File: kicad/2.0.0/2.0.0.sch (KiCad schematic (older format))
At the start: 66 parts

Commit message: assignd footprints to schematic, grouped footprints in pcb designer
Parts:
- C1, C10, C11, C12, C13, C14, C15, C16, C17, C18, C2, C3, C4, C5, C6, C9: renamed from C?; footprint (none) -> Capacitor_SMD:C_0603_1608Metric
- C7, C8: renamed from C?; footprint (none) -> Capacitor_SMD:C_1206_3216Metric
- D1: renamed from D?; footprint (none) -> Sensor_Optical_Position:S5990; symbol Sensor_Optical_Position:S599x -> 2.0.0-rescue:S599x-Sensor_Optical_Position
- J1, J2, J4: renamed from J?; footprint (none) -> Connector_SMA:SMA_Molex_73251-2120_EdgeMount
- J3: renamed from J?; footprint (none) -> TerminalBlock_TE-Connectivity:TerminalBlock_TE_282834-3_1x03_P2.54mm_Horizontal
- R1, R10, R11, R12, R13, R14, R15, R16, R17, R18, R19, R2, R20, R21, R22, R23, R24, R25, R26, R3, R4, R5, R6, R7, R8, R9: renamed from R?; footprint (none) -> Resistor_SMD:R_0603_1608Metric
- U1, U2, U5, U6: renamed from U?; footprint (none) -> Package_SO:SOIC-8_3.9x4.9mm_P1.27mm
- U3: renamed from U?; footprint (none) -> Package_TO_SOT_SMD:SOT-223-3_TabPin2
- gave numbers to parts that had none: 1

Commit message: updated footprints of S5990, OPA197 and OPA2197
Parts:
- removed U1, U2, U5: OPA2197, Package_SO:SOIC-8_3.9x4.9mm_P1.27mm, symbol Device:Opamp_Dual_Generic
- removed U6: OPA197, Package_SO:SOIC-8_3.9x4.9mm_P1.27mm, symbol Device:Opamp_Dual_Generic
- added U1, U2, U5: OPA2197IDR, Package_SO:SOIC-8_3.9x4.9mm_P1.27mm, symbol Amplifier_Operational:OPA2197IDR
- added U6: OPA197IDR, Package_SO:SOIC-8_3.9x4.9mm_P1.27mm, symbol Amplifier_Operational:OPA197IDR
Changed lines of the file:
@@
-	1    0    0    -1
-$EndComp
-$Comp
-L Device:Opamp_Dual_Generic U1
-U 1 1 5E395987
-P 2250 1850
-F 0 "U1" H 2250 1483 50  0000 C CNN
-F 1 "OPA2197" H 2250 1574 50  0000 C CNN
-F 2 "Package_SO:SOIC-8_3.9x4.9mm_P1.27mm" H 2250 1850 50  0001 C CNN
-F 3 "~" H 2250 1850 50  0001 C CNN
-	1    2250 1850
-	1    0    0    1
-$EndComp
-$Comp
-L Device:Opamp_Dual_Generic U1
-U 2 1 5E396064
-P 3750 1850
-F 0 "U1" H 3750 1483 50  0000 C CNN
-F 1 "OPA2197" H 3750 1574 50  0000 C CNN
-F 2 "Package_SO:SOIC-8_3.9x4.9mm_P1.27mm" H 3750 1850 50  0001 C CNN
-F 3 "~" H 3750 1850 50  0001 C CNN
-	2    3750 1850
-	1    0    0    1
-$EndComp
-$Comp
-L Device:Opamp_Dual_Generic U1
-U 3 1 5E39666A
-P 950 1550
-F 0 "U1" H 1000 1650 50  0000 L CNN
-F 1 "OPA2197" H 900 1550 50  0000 L CNN
-F 2 "Package_SO:SOIC-8_3.9x4.9mm_P1.27mm" H 950 1550 50  0001 C CNN
-F 3 "~" H 950 1550 50  0001 C CNN
-	3    950  1550
 	1    0    0    -1
 $EndComp
@@
 Wire Wire Line
 	850  3850 850  3700
-$Comp
-L Device:Opamp_Dual_Generic U2
-U 1 1 5E3E1751
-P 2250 3600
-F 0 "U2" H 2250 3233 50  0000 C CNN
-F 1 "OPA2197" H 2250 3324 50  0000 C CNN
-F 2 "Package_SO:SOIC-8_3.9x4.9mm_P1.27mm" H 2250 3600 50  0001 C CNN
-F 3 "~" H 2250 3600 50  0001 C CNN
-	1    2250 3600
-	1    0    0    1
-$EndComp
-$Comp
-L Device:Opamp_Dual_Generic U2
-U 2 1 5E3E290A
-P 3750 3600
-F 0 "U2" H 3750 3233 50  0000 C CNN
-F 1 "OPA2197" H 3750 3324 50  0000 C CNN
-F 2 "Package_SO:SOIC-8_3.9x4.9mm_P1.27mm" H 3750 3600 50  0001 C CNN
-F 3 "~" H 3750 3600 50  0001 C CNN
-	2    3750 3600
-	1    0    0    1
-$EndComp
-$Comp
-L Device:Opamp_Dual_Generic U2
-U 3 1 5E3E3958
-P 950 3300
-F 0 "U2" H 1000 3400 50  0000 L CNN
-F 1 "OPA2197" H 900 3300 50  0000 L CNN
-F 2 "Package_SO:SOIC-8_3.9x4.9mm_P1.27mm" H 950 3300 50  0001 C CNN
-F 3 "~" H 950 3300 50  0001 C CNN
-	3    950  3300
-	1    0    0    -1
-$EndComp
 Wire Wire Line
 	1200 4550 1000 4550
@@
 Text Notes 2200 4650 0    42   Italic 0
 For details on how to size the feedback capacitor check\nW. Jung. Opamp Application Handbook. p. 273
-$Comp
-L Device:Opamp_Dual_Generic U5
-U 1 1 5E43D5EA
-P 6950 1500
-F 0 "U5" H 6950 1133 50  0000 C CNN
-F 1 "OPA2197" H 6950 1224 50  0000 C CNN
-F 2 "Package_SO:SOIC-8_3.9x4.9mm_P1.27mm" H 6950 1500 50  0001 C CNN
-F 3 "~" H 6950 1500 50  0001 C CNN
-	1    6950 1500
-	1    0    0    1
-$EndComp
-$Comp
-L Device:Opamp_Dual_Generic U5
-U 2 1 5E43E84F
-P 6950 3300
-F 0 "U5" H 6950 2933 50  0000 C CNN
-F 1 "OPA2197" H 6950 3024 50  0000 C CNN
-F 2 "Package_SO:SOIC-8_3.9x4.9mm_P1.27mm" H 6950 3300 50  0001 C CNN
-F 3 "~" H 6950 3300 50  0001 C CNN
-	2    6950 3300
-	1    0    0    1
-$EndComp
-$Comp
-L Device:Opamp_Dual_Generic U5
-U 3 1 5E43F028
-P 5300 2500
-F 0 "U5" H 5050 2450 50  0000 R CNN
-F 1 "OPA2197" H 5100 2550 50  0000 R CNN
-F 2 "Package_SO:SOIC-8_3.9x4.9mm_P1.27mm" H 5300 2500 50  0001 C CNN
-F 3 "~" H 5300 2500 50  0001 C CNN
-	3    5300 2500
-	-1   0    0    1
-$EndComp
 $Comp
 L power:GND #PWR0117
@@
 Text Notes 5600 4600 0    42   Italic 0
 See the S5990 datasheet for details on the formula.
-$Comp
-L Device:Opamp_Dual_Generic U6
-U 1 1 5E6E4B30
-P 10200 1600
-F 0 "U6" H 10200 1233 50  0000 C CNN
-F 1 "OPA197" H 10200 1324 50  0000 C CNN
-F 2 "Package_SO:SOIC-8_3.9x4.9mm_P1.27mm" H 10200 1600 50  0001 C CNN
-F 3 "~" H 10200 1600 50  0001 C CNN
-	1    10200 1600
-	1    0    0    1
-$EndComp
 Text Label 9200 1100 0    50   Italic 0
 -X1
@@
 See the S5990 datasheet for details on the formula.
 Connection ~ 10600 1600
-$Comp
-L Device:Opamp_Dual_Generic U6
-U 3 1 5E764FFA
-P 8700 1950
-F 0 "U6" H 8658 1996 50  0000 L CNN
-F 1 "OPA197" H 8658 1905 50  0000 L CNN
-F 2 "Package_SO:SOIC-8_3.9x4.9mm_P1.27mm" H 8700 1950 50  0001 C CNN
-F 3 "~" H 8700 1950 50  0001 C CNN
-	3    8700 1950
-	1    0    0    -1
-$EndComp
 $Comp
 L power:+12V #PWR0129
@@
 Text Notes 3550 6750 0    50   ~ 0
 OUTPUT CONNECTORS
+$Comp
+L Amplifier_Operational:OPA197IDR U6
+U 2 1 5E3ED93E
+P 8600 1950
+F 0 "U6" H 8850 2000 50  0000 C CNN
+F 1 "OPA197IDR" H 8850 1900 50  0000 C CNN
+F 2 "Package_SO:SOIC-8_3.9x4.9mm_P1.27mm" H 8650 1950 50  0001 C CNN
+F 3 "" H 8650 1950 50  0001 C CNN
+	2    8600 1950
+	1    0    0    -1
+$EndComp
+$Comp
+L Amplifier_Operational:OPA197IDR U6
+U 1 1 5E3EEBF9
+P 10150 1600
+F 0 "U6" H 10250 1750 50  0000 L CNN
+F 1 "OPA197IDR" H 10200 1400 50  0000 L CNN
+F 2 "Package_SO:SOIC-8_3.9x4.9mm_P1.27mm" H 10200 1600 50  0001 C CNN
+F 3 "" H 10200 1600 50  0001 C CNN
+	1    10150 1600
+	1    0    0    -1
+$EndComp
+$Comp
+L Amplifier_Operational:OPA2197IDR U5
+U 2 1 5E495054
+P 6900 3300
+F 0 "U5" H 7100 3450 50  0000 C CNN
+F 1 "OPA2197IDR" H 7100 3100 50  0000 C CNN
+F 2 "Package_SO:SOIC-8_3.9x4.9mm_P1.27mm" H 6950 3500 50  0001 C CNN
+F 3 "~" H 6950 3500 50  0001 C CNN
+	2    6900 3300
+	1    0    0    -1
+$EndComp
+$Comp
+L Amplifier_Operational:OPA2197IDR U5
+U 3 1 5E4964C0
+P 5500 2500
+F 0 "U5" H 5600 2550 50  0000 L CNN
+F 1 "OPA2197IDR" H 5458 2455 50  0000 L CNN
+F 2 "Package_SO:SOIC-8_3.9x4.9mm_P1.27mm" H 5550 2700 50  0001 C CNN
+F 3 "~" H 5550 2700 50  0001 C CNN
+	3    5500 2500
+	1    0    0    -1
+$EndComp
+$Comp
+L Amplifier_Operational:OPA2197IDR U1
+U 1 1 5E4983D9
+P 2200 1850
+F 0 "U1" H 2350 2050 50  0000 C CNN
+F 1 "OPA2197IDR" H 2450 1650 50  0000 C CNN
+F 2 "Package_SO:SOIC-8_3.9x4.9mm_P1.27mm" H 2250 2050 50  0001 C CNN
+F 3 "~" H 2250 2050 50  0001 C CNN
+	1    2200 1850
+	1    0    0    -1
+$EndComp
+$Comp
+L Amplifier_Operational:OPA2197IDR U1
+U 2 1 5E4995C9
+P 3700 1850
+F 0 "U1" H 3850 2050 50  0000 C CNN
+F 1 "OPA2197IDR" H 3950 1650 50  0000 C CNN
+F 2 "Package_SO:SOIC-8_3.9x4.9mm_P1.27mm" H 3750 2050 50  0001 C CNN
+F 3 "~" H 3750 2050 50  0001 C CNN
+	2    3700 1850
+	1    0    0    -1
+$EndComp
+$Comp
+L Amplifier_Operational:OPA2197IDR U1
+U 3 1 5E49A8CC
+P 950 1550
+F 0 "U1" H 1050 1650 50  0000 L CNN
+F 1 "OPA2197IDR" H 900 1550 50  0000 L CNN
+F 2 "Package_SO:SOIC-8_3.9x4.9mm_P1.27mm" H 1000 1750 50  0001 C CNN
+F 3 "~" H 1000 1750 50  0001 C CNN
+	3    950  1550
+	1    0    0    -1
+$EndComp
+$Comp
+L Amplifier_Operational:OPA2197IDR U2
+U 1 1 5E4A737B
+P 2200 3600
+F 0 "U2" H 2350 3800 50  0000 C CNN
+F 1 "OPA2197IDR" H 2500 3400 50  0000 C CNN
+F 2 "Package_SO:SOIC-8_3.9x4.9mm_P1.27mm" H 2250 3800 50  0001 C CNN
+F 3 "~" H 2250 3800 50  0001 C CNN
+	1    2200 3600
+	1    0    0    -1
+$EndComp
+$Comp
+L Amplifier_Operational:OPA2197IDR U2
+U 2 1 5E4A876E
+P 3700 3600
+F 0 "U2" H 3800 3800 50  0000 C CNN
+F 1 "OPA2197IDR" H 4000 3400 50  0000 C CNN
+F 2 "Package_SO:SOIC-8_3.9x4.9mm_P1.27mm" H 3750 3800 50  0001 C CNN
+F 3 "~" H 3750 3800 50  0001 C CNN
+	2    3700 3600
+	1    0    0    -1
+$EndComp
+$Comp
+L Amplifier_Operational:OPA2197IDR U2
+U 3 1 5E4A97F1
+P 950 3300
+F 0 "U2" H 1050 3450 50  0000 L CNN
+F 1 "OPA2197IDR" H 950 3350 50  0000 L CNN
+F 2 "Package_SO:SOIC-8_3.9x4.9mm_P1.27mm" H 1000 3500 50  0001 C CNN
+F 3 "~" H 1000 3500 50  0001 C CNN
+	3    950  3300
+	1    0    0    -1
+$EndComp
+$Comp
+L Amplifier_Operational:OPA2197IDR U5
+U 1 1 5E493BA7
+P 6900 1500
+F 0 "U5" H 7100 1650 50  0000 C CNN
+F 1 "OPA2197IDR" H 7150 1300 50  0000 C CNN
+F 2 "Package_SO:SOIC-8_3.9x4.9mm_P1.27mm" H 6950 1700 50  0001 C CNN
+F 3 "~" H 6950 1700 50  0001 C CNN
+	1    6900 1500
+	1    0    0    -1
+$EndComp
 $EndSCHEMATC

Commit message: updated S5990 symbol to show pin number
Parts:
- removed D1: S599x, Sensor_Optical_Position:S5990, symbol 2.0.0-rescue:S599x-Sensor_Optical_Position
- added D1: S599x, Sensor_Optical_Position:S5990, symbol Sensor_Optical_Position:S599x

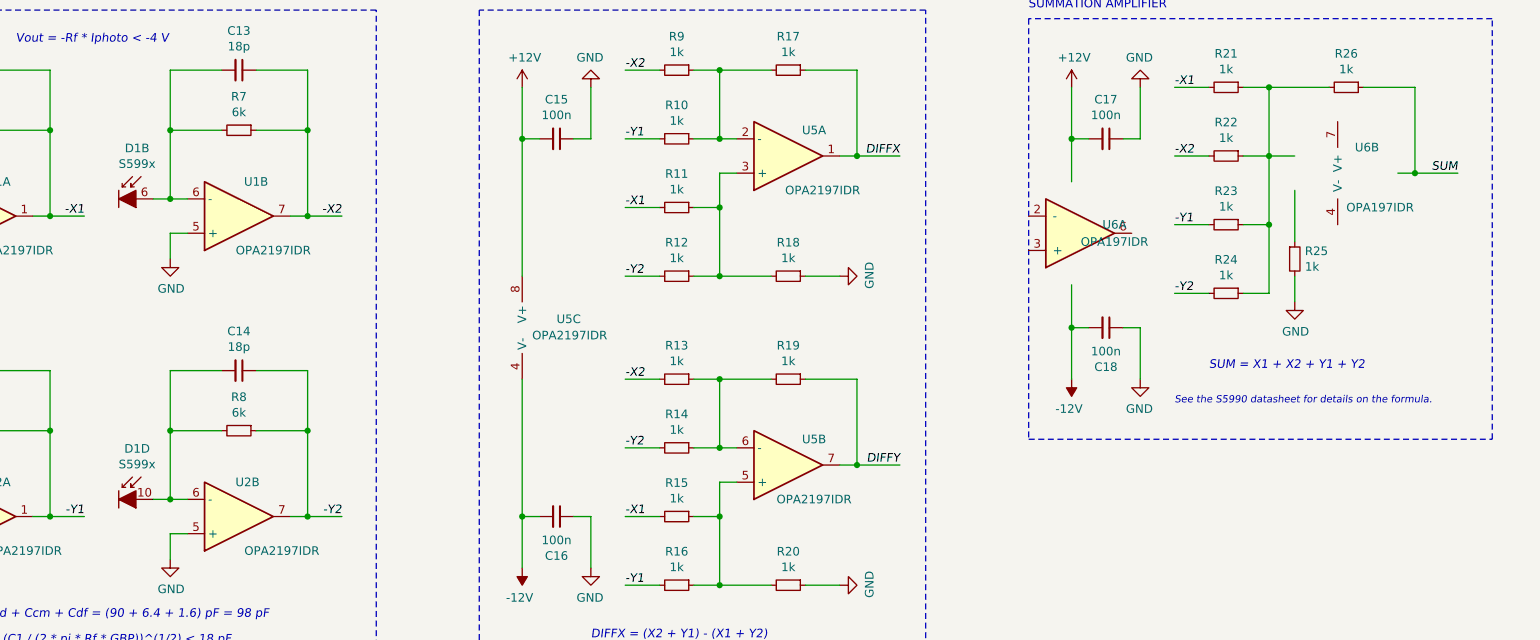
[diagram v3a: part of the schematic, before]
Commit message: grouped components for 2.0.0 design on pcb
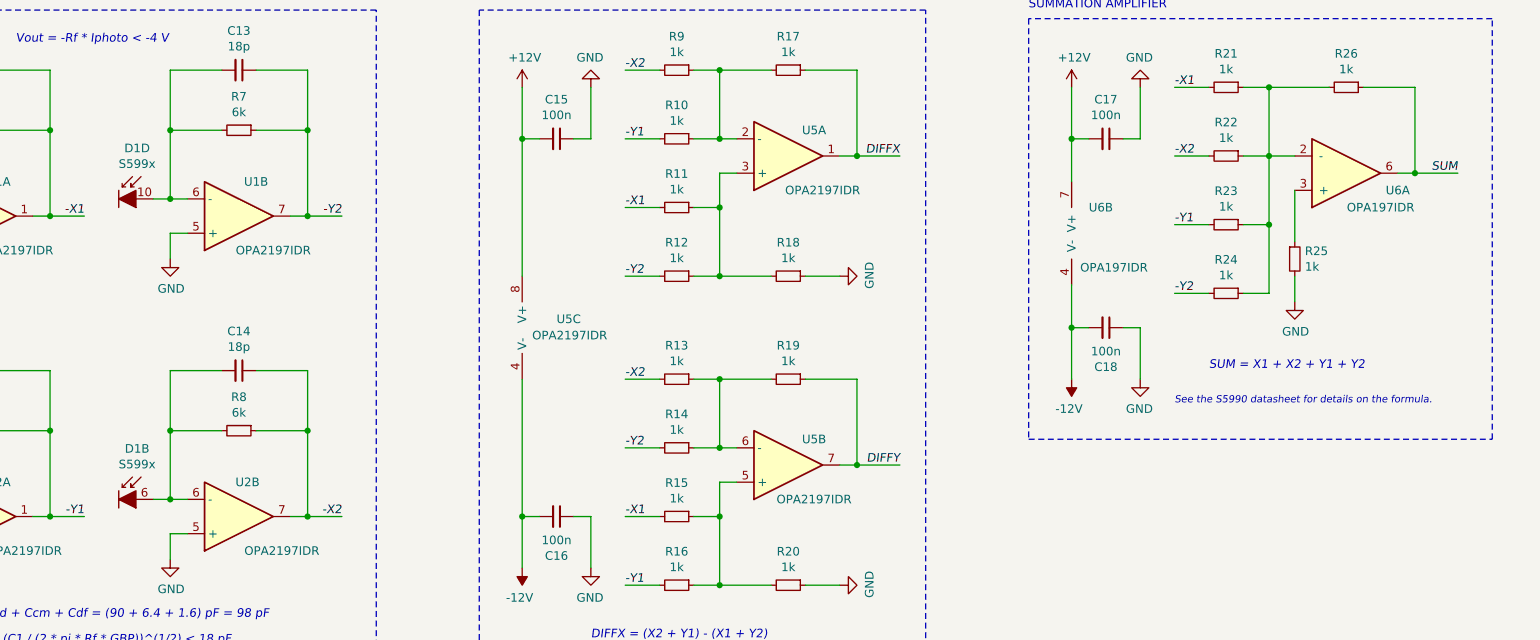
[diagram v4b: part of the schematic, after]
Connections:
- net +12V: now also U6.7 (V+)
- net -12V: now also U6.4 (V-)
- net -X2: now also C14.1, R8.1, U2.7; no longer C13.1, R7.1, U1.7
- net -Y2: now also C13.1, R7.1, U1.7; no longer C14.1, R8.1, U2.7
- net SUM: now also U6.6
- net at C13.2, R7.2, U1.6 (-): now also D1.10 (Anode_Y2); no longer D1.6 (Anode_X2)
- net at C14.2, R8.2, U2.6 (-): now also D1.6 (Anode_X2); no longer D1.10 (Anode_Y2)
- net at U6.2 (-): now also R21.1, R22.1, R23.1, R24.1, R26.2
- net at U6.3 (+): now also R25.1
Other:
- moved on the sheet: D1B, D1D, U6A, U6B
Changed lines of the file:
@@
 	3350 1950 3350 2100
 Text Label 4350 1850 2    50   Italic 0
--X2
+-Y2
 Wire Wire Line
 	4350 1850 4150 1850
@@
 	3350 3700 3350 3850
 Text Label 4350 3600 2    50   Italic 0
--Y2
+-X2
 Wire Wire Line
 	4350 3600 4150 3600
@@
 L Amplifier_Operational:OPA197IDR U6
 U 1 1 5E3ED93E
+P 10150 1600
+F 0 "U6" H 10500 1500 50  0000 C CNN
+F 1 "OPA197IDR" H 10400 1400 50  0000 C CNN
+F 2 "Package_SO:SOIC-8_3.9x4.9mm_P1.27mm" H 10200 1600 50  0001 C CNN
+F 3 "" H 10200 1600 50  0001 C CNN
+	1    10150 1600
+	1    0    0    -1
+$EndComp
+$Comp
+L Amplifier_Operational:OPA197IDR U6
+U 2 1 5E3EEBF9
 P 8600 1950
-F 0 "U6" H 8850 2000 50  0000 C CNN
-F 1 "OPA197IDR" H 8850 1900 50  0000 C CNN
+F 0 "U6" H 8700 2100 50  0000 L CNN
+F 1 "OPA197IDR" H 8650 1750 50  0000 L CNN
 F 2 "Package_SO:SOIC-8_3.9x4.9mm_P1.27mm" H 8650 1950 50  0001 C CNN
 F 3 "" H 8650 1950 50  0001 C CNN
-	1    8600 1950
-	1    0    0    -1
-$EndComp
-$Comp
-L Amplifier_Operational:OPA197IDR U6
-U 2 1 5E3EEBF9
-P 10150 1600
-F 0 "U6" H 10250 1750 50  0000 L CNN
-F 1 "OPA197IDR" H 10200 1400 50  0000 L CNN
-F 2 "Package_SO:SOIC-8_3.9x4.9mm_P1.27mm" H 10200 1600 50  0001 C CNN
-F 3 "" H 10200 1600 50  0001 C CNN
-	2    10150 1600
+	2    8600 1950
 	1    0    0    -1
 $EndComp
@@
 L Sensor_Optical_Position:S599x D1
 U 2 1 5E415FEF
-P 3150 1750
-F 0 "D1" H 3157 2045 50  0000 C CNN
-F 1 "S599x" H 3157 1954 50  0000 C CNN
-F 2 "Sensor_Optical_Position:S5990" H 3100 1750 50  0001 C CNN
-F 3 "" H 3100 1750 50  0001 C CNN
-	2    3150 1750
+P 3150 3500
+F 0 "D1" H 3157 3795 50  0000 C CNN
+F 1 "S599x" H 3157 3704 50  0000 C CNN
+F 2 "Sensor_Optical_Position:S5990" H 3100 3500 50  0001 C CNN
+F 3 "" H 3100 3500 50  0001 C CNN
+	2    3150 3500
 	1    0    0    -1
 $EndComp
@@
 L Sensor_Optical_Position:S599x D1
 U 4 1 5E41858C
-P 3150 3500
-F 0 "D1" H 3157 3795 50  0000 C CNN
-F 1 "S599x" H 3157 3704 50  0000 C CNN
-F 2 "Sensor_Optical_Position:S5990" H 3100 3500 50  0001 C CNN
-F 3 "" H 3100 3500 50  0001 C CNN
-	4    3150 3500
-	1    0    0    -1
-$EndComp
+P 3150 1750
+F 0 "D1" H 3157 2045 50  0000 C CNN
+F 1 "S599x" H 3157 1954 50  0000 C CNN
+F 2 "Sensor_Optical_Position:S5990" H 3100 1750 50  0001 C CNN
+F 3 "" H 3100 1750 50  0001 C CNN
+	4    3150 1750
+	1    0    0    -1
+$EndComp
